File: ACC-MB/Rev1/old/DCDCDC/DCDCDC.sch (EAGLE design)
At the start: 21 parts, among them X2 5566-4

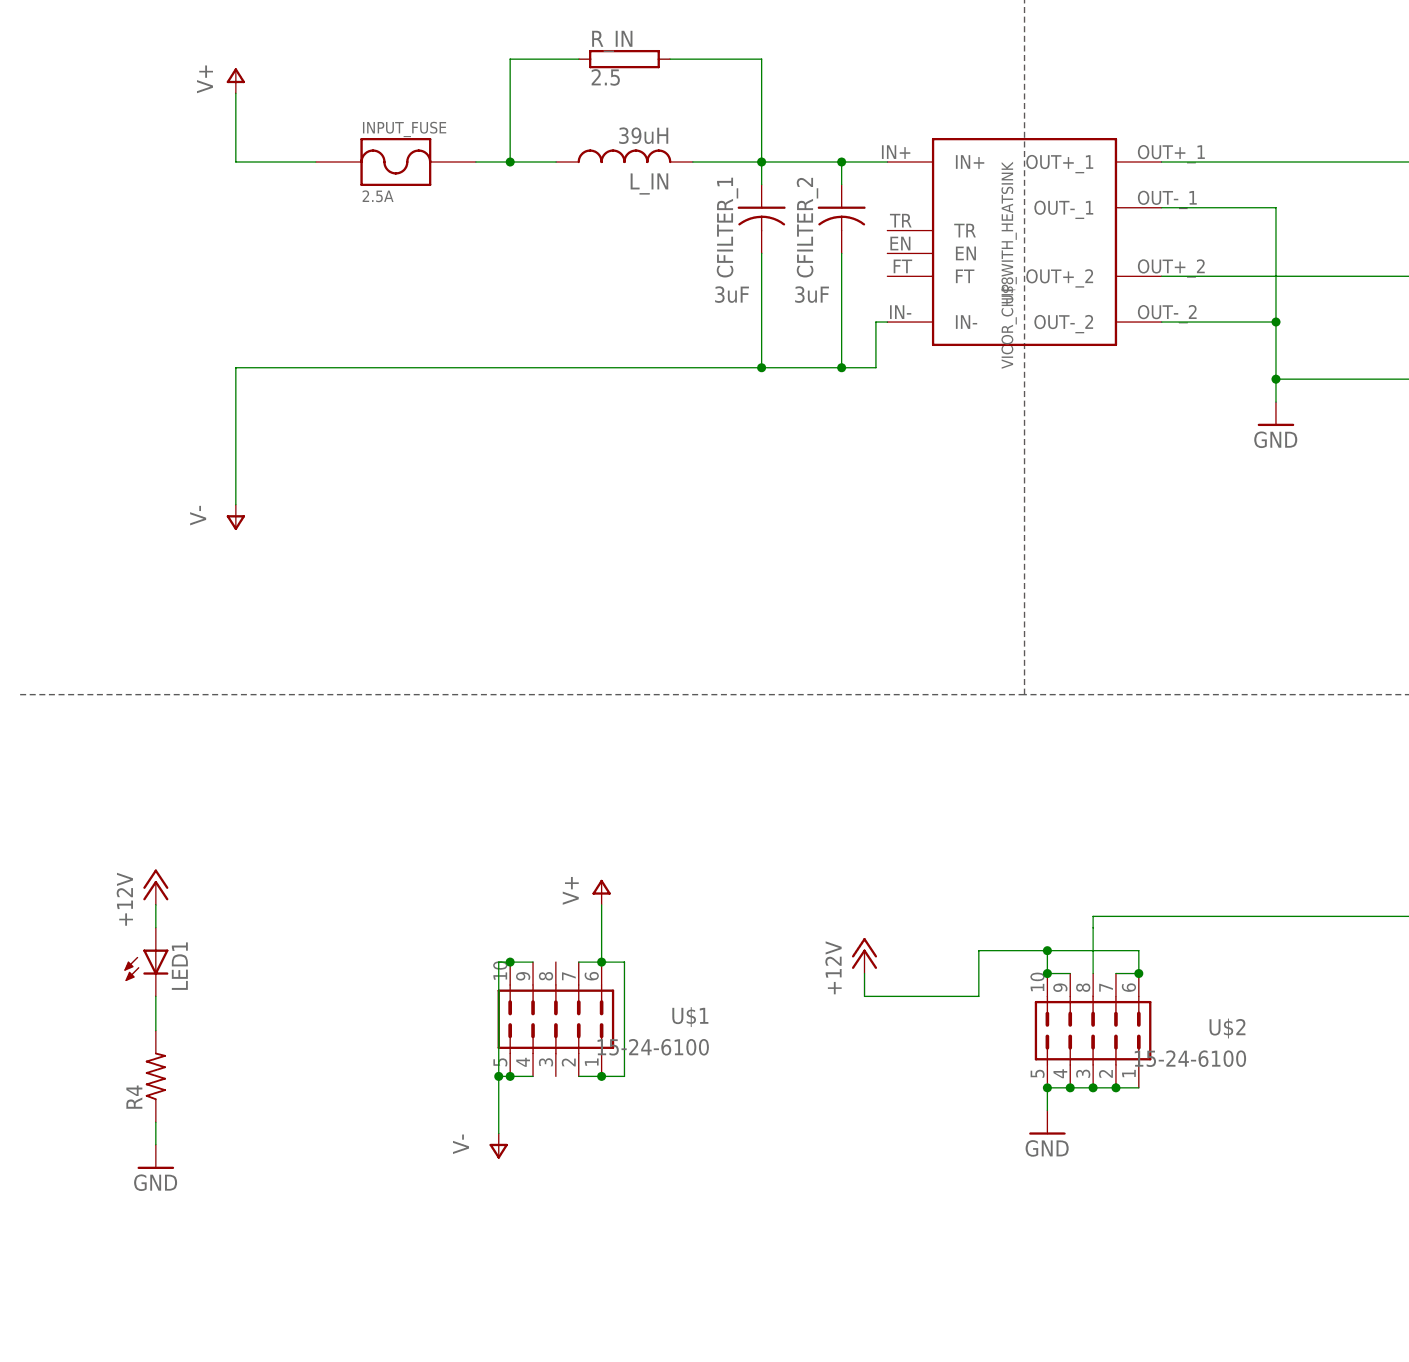
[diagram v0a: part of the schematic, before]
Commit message: 7792 added to all DC
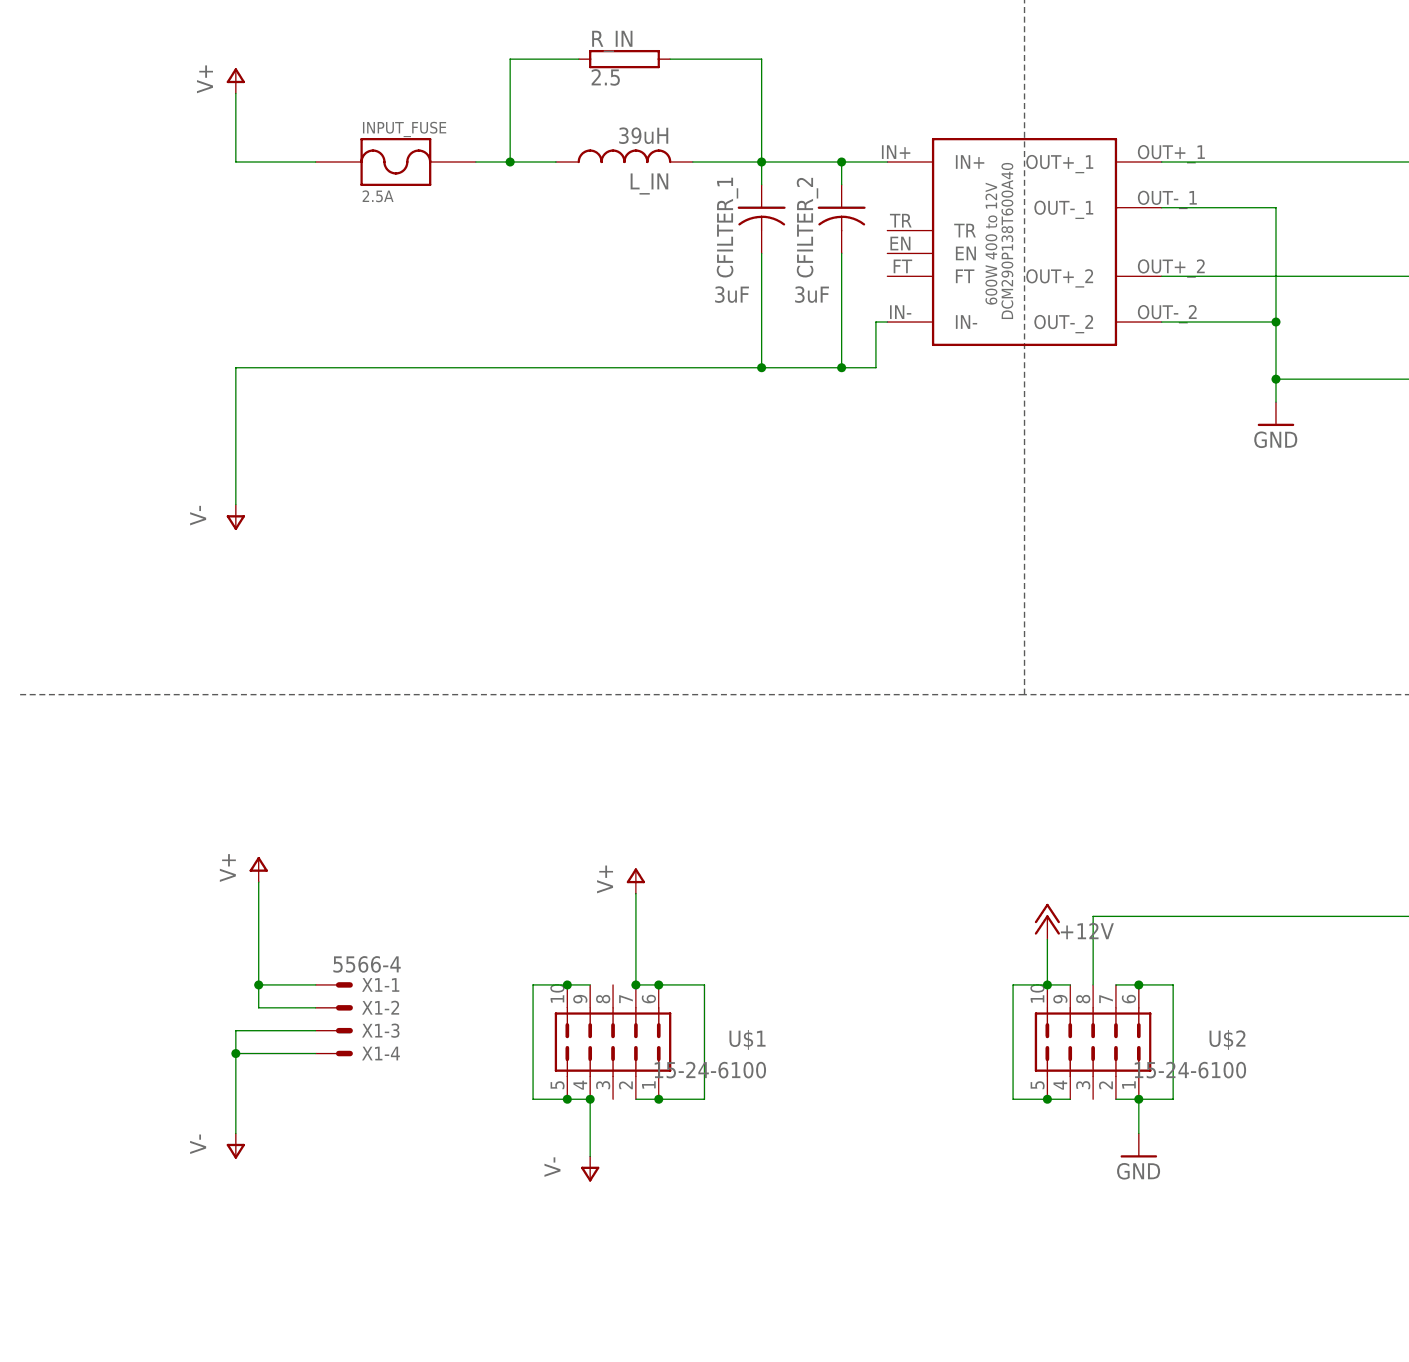
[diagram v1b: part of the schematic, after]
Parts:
- removed LED1: (no value), ACC-MB-R0:LED3MM
- removed R4: (no value), ACC-MB-R0:R-US_R0805
- added X1: 5566-4, ACC-MB-R0:5566-4
- DCM290P138T600A40: value VICOR_CHIP_WITH_HEATSINK -> 600W 400 to 12V
- renumbered U$8 to DCM290P138T600A40
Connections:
- removed net N$5: LED1.C, R4.2
- net +12V: now also U$2.4, U$2.5; no longer LED1.A, U$2.6, U$2.7
- net GND: now also U$2.6, U$2.7; no longer R4.1, U$2.3, U$2.4, U$2.5
- net V+: now also X1-1.S, X1-2.S
- net V-: now also X1-3.S, X1-4.S
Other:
- moved on the sheet: U$1, U$2
